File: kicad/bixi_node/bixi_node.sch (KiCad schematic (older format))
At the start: 6 parts, among them J1 RJ45, J2 Screw_Terminal_1x02, P1 CONN_01X03, U1 SP3485CN

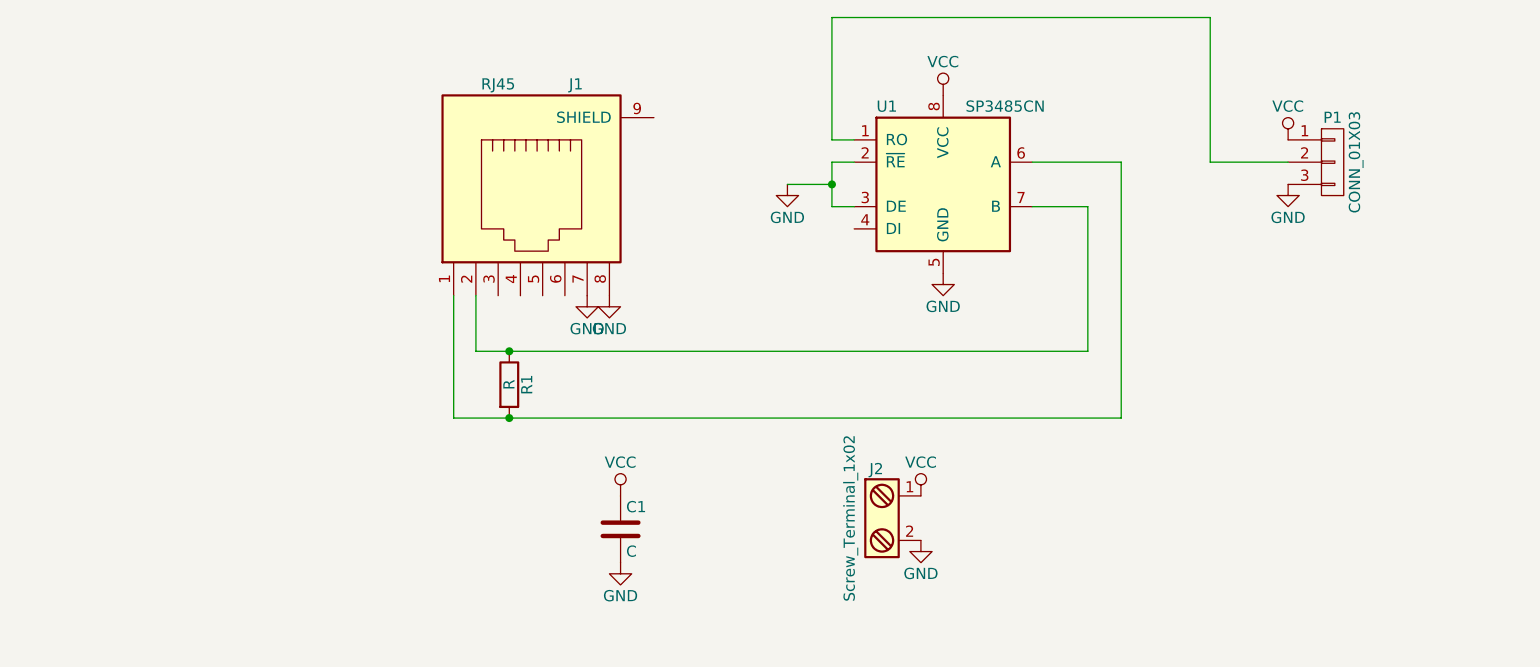
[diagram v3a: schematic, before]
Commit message: both pcb's sent to fab
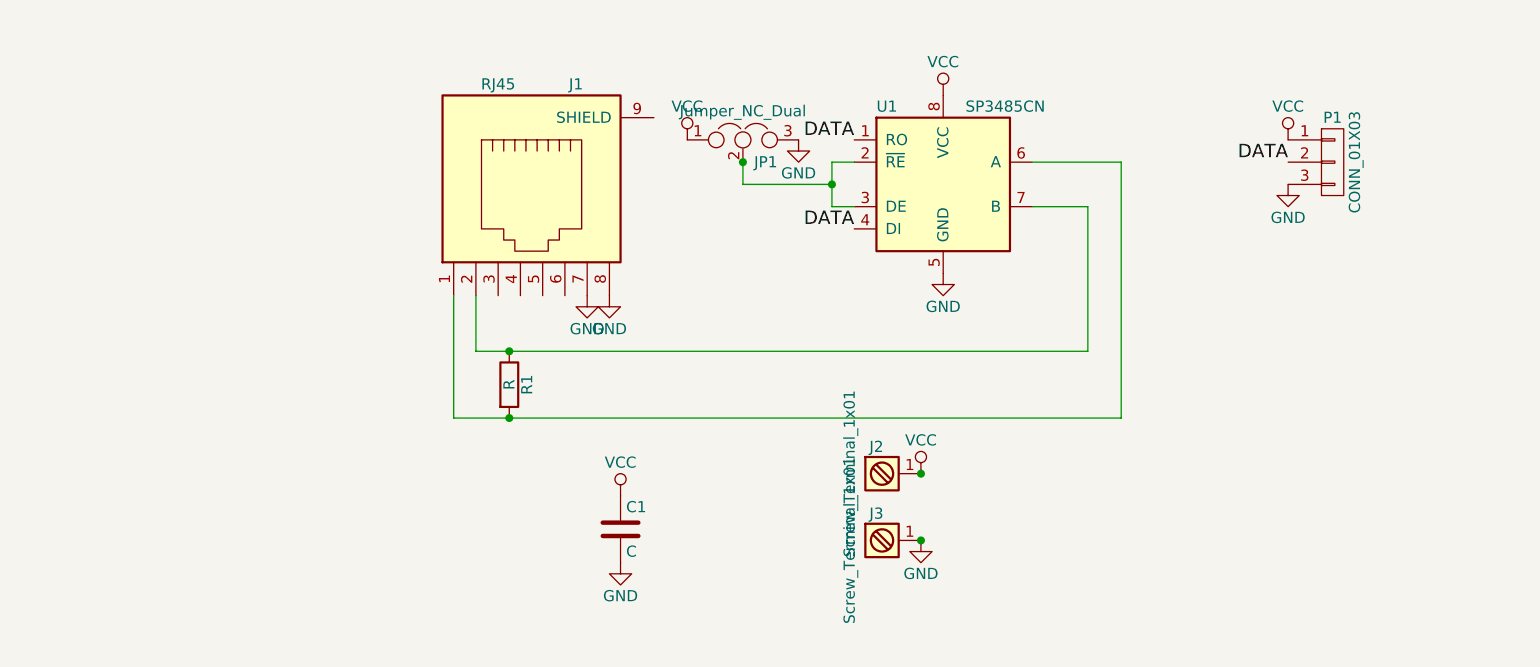
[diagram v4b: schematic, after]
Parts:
- removed J2: Screw_Terminal_1x02, custom:HB9500-2P, symbol Screw_Terminal_1x02
- added J2, J3: Screw_Terminal_1x01, custom:A116169CT_SPADE_CONNECTOR, symbol Screw_Terminal_1x01
- added JP1: Jumper_NC_Dual, custom:jumper_3_pin_fixed, symbol Jumper_NC_Dual
- P1: footprint custom:PAD_3X_OVAL -> custom:PAD_3X_OVAL_WS2812B
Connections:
- net GND: now also J3.1, JP1.3; no longer U1.2 (~RE~), U1.3 (DE)
- net VCC: now also J2.1, JP1.1
- net DATA: now reaches P1.2 (P2), U1.1 (RO)
- net DATA: now also U1.4 (DI)
- new net: JP1.2, U1.2 (~RE~), U1.3 (DE)
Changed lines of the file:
@@
+	1    0    0    -1
+$EndComp
+$Comp
+L VCC #PWR07
+U 1 1 58D6B5B6
+P 7350 3100
+F 0 "#PWR07" H 7350 2950 50  0001 C CNN
+F 1 "VCC" H 7350 3250 50  0000 C CNN
+F 2 "" H 7350 3100 50  0000 C CNN
+F 3 "" H 7350 3100 50  0000 C CNN
+	1    7350 3100
+	1    0    0    -1
+$EndComp
+$Comp
+L GND #PWR08
+U 1 1 58D6B5DA
+P 7350 3300
+F 0 "#PWR08" H 7350 3050 50  0001 C CNN
+F 1 "GND" H 7350 3150 50  0000 C CNN
+F 2 "" H 7350 3300 50  0000 C CNN
+F 3 "" H 7350 3300 50  0000 C CNN
+	1    7350 3300
+	1    0    0    -1
+$EndComp
+$Comp
+L GND #PWR09
+U 1 1 58D6B6AE
+P 5700 4900
+F 0 "#PWR09" H 5700 4650 50  0001 C CNN
+F 1 "GND" H 5700 4750 50  0000 C CNN
+F 2 "" H 5700 4900 50  0000 C CNN
+F 3 "" H 5700 4900 50  0000 C CNN
+	1    5700 4900
+	1    0    0    -1
+$EndComp
+$Comp
+L VCC #PWR010
+U 1 1 58D6B70F
+P 5700 4600
+F 0 "#PWR010" H 5700 4450 50  0001 C CNN
+F 1 "VCC" H 5700 4750 50  0000 C CNN
+F 2 "" H 5700 4600 50  0000 C CNN
+F 3 "" H 5700 4600 50  0000 C CNN
+	1    5700 4600
+	1    0    0    -1
+$EndComp
+$Comp
+L CONN_01X03 P1
+U 1 1 58D6C384
+P 7550 3200
+F 0 "P1" H 7550 3400 50  0000 C CNN
+F 1 "CONN_01X03" V 7650 3200 50  0000 C CNN
+F 2 "custom:PAD_3X_OVAL_WS2812B" H 7550 3200 50  0001 C CNN
+F 3 "" H 7550 3200 50  0000 C CNN
+	1    7550 3200
+	1    0    0    -1
+$EndComp
+$Comp
+L Screw_Terminal_1x01 J2
+U 1 1 58EA38FE
+P 5500 4600
+F 0 "J2" H 5500 4750 50  0000 C TNN
+F 1 "Screw_Terminal_1x01" V 5350 4600 50  0000 C TNN
+F 2 "custom:A116169CT_SPADE_CONNECTOR" H 5500 4475 50  0001 C CNN
+F 3 "" H 5500 4500 50  0001 C CNN
+	1    5500 4600
+	1    0    0    -1
+$EndComp
+$Comp
+L Screw_Terminal_1x01 J3
+U 1 1 58EA3975
+P 5500 4900
+F 0 "J3" H 5500 5050 50  0000 C TNN
+F 1 "Screw_Terminal_1x01" V 5350 4900 50  0000 C TNN
+F 2 "custom:A116169CT_SPADE_CONNECTOR" H 5500 4775 50  0001 C CNN
+F 3 "" H 5500 4800 50  0001 C CNN
+	1    5500 4900
+	1    0    0    -1
+$EndComp
+$Comp
+L VCC #PWR011
+U 1 1 58EA51F3
+P 4650 3100
+F 0 "#PWR011" H 4650 2950 50  0001 C CNN
+F 1 "VCC" H 4650 3250 50  0000 C CNN
+F 2 "" H 4650 3100 50  0000 C CNN
+F 3 "" H 4650 3100 50  0000 C CNN
+	1    4650 3100
+	1    0    0    -1
+$EndComp
+$Comp
+L GND #PWR012
+U 1 1 58EA5217
+P 5150 3100
+F 0 "#PWR012" H 5150 2850 50  0001 C CNN
+F 1 "GND" H 5150 2950 50  0000 C CNN
+F 2 "" H 5150 3100 50  0000 C CNN
+F 3 "" H 5150 3100 50  0000 C CNN
+	1    5150 3100
 	1    0    0    -1
 $EndComp
@@
 Connection ~ 5300 3300
 Wire Wire Line
-	5400 3100 5300 3100
+	4900 3300 5300 3300
+Connection ~ 3850 4050
+Connection ~ 3850 4350
+Connection ~ 5700 4900
+Connection ~ 5700 4600
 Wire Wire Line
-	5300 3100 5300 2550
-Wire Wire Line
-	5300 2550 7000 2550
-Wire Wire Line
-	7000 2550 7000 3200
-Wire Wire Line
-	7000 3200 7350 3200
+	4900 3300 4900 3200
+Text Label 7350 3200 2    60   ~ 0
+DATA
+Text Label 5400 3100 2    60   ~ 0
+DATA
+Text Label 5400 3500 2    60   ~ 0
+DATA
+Connection ~ 4900 3200
 $Comp
-L GND #PWR07
-U 1 1 58CE0E7E
-P 5100 3300
-F 0 "#PWR07" H 5100 3050 50  0001 C CNN
-F 1 "GND" H 5100 3150 50  0000 C CNN
-F 2 "" H 5100 3300 50  0000 C CNN
-F 3 "" H 5100 3300 50  0000 C CNN
-	1    5100 3300
+L Jumper_NC_Dual JP1
+U 1 1 58EA59A3
+P 4900 3100
+F 0 "JP1" H 4950 3000 50  0000 L CNN
+F 1 "Jumper_NC_Dual" H 4900 3200 50  0000 C BNN
+F 2 "custom:jumper_3_pin_fixed" H 4900 3100 50  0001 C CNN
+F 3 "" H 4900 3100 50  0000 C CNN
+	1    4900 3100
 	1    0    0    -1
 $EndComp
-Wire Wire Line
-	5300 3300 5100 3300
-$Comp
-L VCC #PWR08
-U 1 1 58D6B5B6
-P 7350 3100
-F 0 "#PWR08" H 7350 2950 50  0001 C CNN
-F 1 "VCC" H 7350 3250 50  0000 C CNN
-F 2 "" H 7350 3100 50  0000 C CNN
-F 3 "" H 7350 3100 50  0000 C CNN
-	1    7350 3100
-	1    0    0    -1
-$EndComp
-$Comp
-L GND #PWR09
-U 1 1 58D6B5DA
-P 7350 3300
-F 0 "#PWR09" H 7350 3050 50  0001 C CNN
-F 1 "GND" H 7350 3150 50  0000 C CNN
-F 2 "" H 7350 3300 50  0000 C CNN
-F 3 "" H 7350 3300 50  0000 C CNN
-	1    7350 3300
-	1    0    0    -1
-$EndComp
-$Comp
-L GND #PWR010
-U 1 1 58D6B6AE
-P 5700 4900
-F 0 "#PWR010" H 5700 4650 50  0001 C CNN
-F 1 "GND" H 5700 4750 50  0000 C CNN
-F 2 "" H 5700 4900 50  0000 C CNN
-F 3 "" H 5700 4900 50  0000 C CNN
-	1    5700 4900
-	1    0    0    -1
-$EndComp
-$Comp
-L VCC #PWR011
-U 1 1 58D6B70F
-P 5700 4700
-F 0 "#PWR011" H 5700 4550 50  0001 C CNN
-F 1 "VCC" H 5700 4850 50  0000 C CNN
-F 2 "" H 5700 4700 50  0000 C CNN
-F 3 "" H 5700 4700 50  0000 C CNN
-	1    5700 4700
-	1    0    0    -1
-$EndComp
-$Comp
-L CONN_01X03 P1
-U 1 1 58D6C384
-P 7550 3200
-F 0 "P1" H 7550 3400 50  0000 C CNN
-F 1 "CONN_01X03" V 7650 3200 50  0000 C CNN
-F 2 "custom:PAD_3X_OVAL" H 7550 3200 50  0001 C CNN
-F 3 "" H 7550 3200 50  0000 C CNN
-	1    7550 3200
-	1    0    0    -1
-$EndComp
-Connection ~ 3850 4050
-Connection ~ 3850 4350
-$Comp
-L Screw_Terminal_1x02 J2
-U 1 1 58E151AB
-P 5500 4800
-F 0 "J2" H 5500 5050 50  0000 C TNN
-F 1 "Screw_Terminal_1x02" V 5350 4800 50  0000 C TNN
-F 2 "custom:HB9500-2P" H 5500 4575 50  0001 C CNN
-F 3 "" H 5475 4800 50  0001 C CNN
-	1    5500 4800
-	1    0    0    -1
-$EndComp

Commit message: v2 pcb
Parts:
- C1: footprint Resistors_THT:Resistor_Horizontal_RM7mm -> Capacitors_THT:C_Disc_D3.0mm_W2.0mm_P2.50mm
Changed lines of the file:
@@
 F 0 "C1" H 4375 4950 50  0000 L CNN
 F 1 "C" H 4375 4750 50  0000 L CNN
-F 2 "Resistors_THT:Resistor_Horizontal_RM7mm" H 4388 4700 50  0001 C CNN
+F 2 "Capacitors_THT:C_Disc_D3.0mm_W2.0mm_P2.50mm" H 4388 4700 50  0001 C CNN
 F 3 "" H 4350 4850 50  0000 C CNN
 	1    4350 4850

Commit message: bixi node updates
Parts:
- C1: footprint Capacitors_THT:C_Disc_D3.0mm_W2.0mm_P2.50mm -> Capacitors_THT:C_Axial_L3.8mm_D2.6mm_P7.50mm_Horizontal
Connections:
- net DATA: now also J1.3
- net VCC: now also J1.5, J1.6
- net DATA_DIFF_A: now reaches J1.1, R1.2, U1.6 (A)
- net DATA_DIFF_B: now reaches J1.2, R1.1, U1.7 (B)
- net MODE: now reaches JP1.2, U1.2 (~RE~), U1.3 (DE)
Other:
- moved on the sheet: J2, J3, JP1, P1

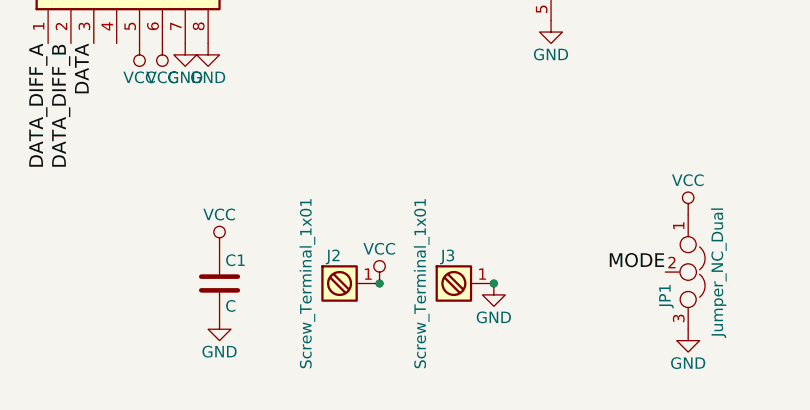
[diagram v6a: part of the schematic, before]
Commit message: v3 boards almost complete. added xcvr breakout, passthrough boards
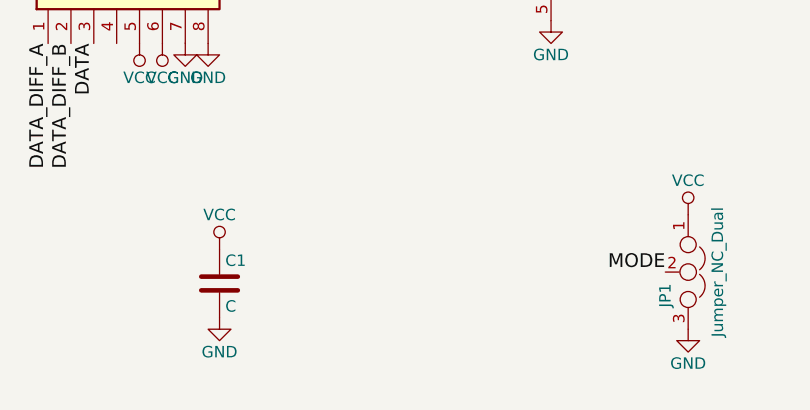
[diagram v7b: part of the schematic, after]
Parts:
- removed J2, J3: Screw_Terminal_1x01, custom:A116169CT_SPADE_CONNECTOR, symbol Screw_Terminal_1x01
- P1: footprint custom:PAD_3X_OVAL_WS2812B -> Connectors_JST:JST_EH_S03B-EH_03x2.50mm_Angled
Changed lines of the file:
@@
 $EndComp
 $Comp
-L GND #PWR10
+L GND #PWR01
 U 1 1 58CE067C
 P 5800 3700
-F 0 "#PWR10" H 5800 3450 50  0001 C CNN
+F 0 "#PWR01" H 5800 3450 50  0001 C CNN
 F 1 "GND" H 5800 3550 50  0000 C CNN
 F 2 "" H 5800 3700 50  0000 C CNN
@@
 $EndComp
 $Comp
-L GND #PWR3
+L GND #PWR02
 U 1 1 58CE0696
 P 4200 3800
-F 0 "#PWR3" H 4200 3550 50  0001 C CNN
+F 0 "#PWR02" H 4200 3550 50  0001 C CNN
 F 1 "GND" H 4200 3650 50  0000 C CNN
 F 2 "" H 4200 3800 50  0000 C CNN
@@
 $EndComp
 $Comp
-L GND #PWR4
+L GND #PWR03
 U 1 1 58CE06B0
 P 4300 3800
-F 0 "#PWR4" H 4300 3550 50  0001 C CNN
+F 0 "#PWR03" H 4300 3550 50  0001 C CNN
 F 1 "GND" H 4300 3650 50  0000 C CNN
 F 2 "" H 4300 3800 50  0000 C CNN
@@
 $EndComp
 $Comp
-L VCC #PWR9
+L VCC #PWR04
 U 1 1 58CE06CA
 P 5800 2900
-F 0 "#PWR9" H 5800 2750 50  0001 C CNN
+F 0 "#PWR04" H 5800 2750 50  0001 C CNN
 F 1 "VCC" H 5800 3050 50  0000 C CNN
 F 2 "" H 5800 2900 50  0000 C CNN
@@
 $EndComp
 $Comp
-L VCC #PWR5
+L VCC #PWR05
 U 1 1 58CE07F1
 P 4350 4700
-F 0 "#PWR5" H 4350 4550 50  0001 C CNN
+F 0 "#PWR05" H 4350 4550 50  0001 C CNN
 F 1 "VCC" H 4350 4850 50  0000 C CNN
 F 2 "" H 4350 4700 50  0000 C CNN
@@
 $EndComp
 $Comp
-L GND #PWR6
+L GND #PWR06
 U 1 1 58CE0C7F
 P 4350 5000
-F 0 "#PWR6" H 4350 4750 50  0001 C CNN
+F 0 "#PWR06" H 4350 4750 50  0001 C CNN
 F 1 "GND" H 4350 4850 50  0000 C CNN
 F 2 "" H 4350 5000 50  0000 C CNN
@@
 $EndComp
 $Comp
-L VCC #PWR13
+L VCC #PWR07
 U 1 1 58D6B5B6
 P 8050 3200
-F 0 "#PWR13" H 8050 3050 50  0001 C CNN
+F 0 "#PWR07" H 8050 3050 50  0001 C CNN
 F 1 "VCC" H 8050 3350 50  0000 C CNN
 F 2 "" H 8050 3200 50  0000 C CNN
@@
 $EndComp
 $Comp
-L GND #PWR14
+L GND #PWR08
 U 1 1 58D6B5DA
 P 8050 3400
-F 0 "#PWR14" H 8050 3150 50  0001 C CNN
+F 0 "#PWR08" H 8050 3150 50  0001 C CNN
 F 1 "GND" H 8050 3250 50  0000 C CNN
 F 2 "" H 8050 3400 50  0000 C CNN
 F 3 "" H 8050 3400 50  0000 C CNN
 	1    8050 3400
-	1    0    0    -1
-$EndComp
-$Comp
-L GND #PWR8
-U 1 1 58D6B6AE
-P 5550 4850
-F 0 "#PWR8" H 5550 4600 50  0001 C CNN
-F 1 "GND" H 5550 4700 50  0000 C CNN
-F 2 "" H 5550 4850 50  0000 C CNN
-F 3 "" H 5550 4850 50  0000 C CNN
-	1    5550 4850
-	1    0    0    -1
-$EndComp
-$Comp
-L VCC #PWR7
-U 1 1 58D6B70F
-P 5050 4850
-F 0 "#PWR7" H 5050 4700 50  0001 C CNN
-F 1 "VCC" H 5050 5000 50  0000 C CNN
-F 2 "" H 5050 4850 50  0000 C CNN
-F 3 "" H 5050 4850 50  0000 C CNN
-	1    5050 4850
 	1    0    0    -1
 $EndComp
@@
 F 0 "P1" H 8250 3500 50  0000 C CNN
 F 1 "CONN_01X03" V 8350 3300 50  0000 C CNN
-F 2 "custom:PAD_3X_OVAL_WS2812B" H 8250 3300 50  0001 C CNN
+F 2 "Connectors_JST:JST_EH_S03B-EH_03x2.50mm_Angled" H 8250 3300 50  0001 C CNN
 F 3 "" H 8250 3300 50  0000 C CNN
 	1    8250 3300
@@
 $EndComp
 $Comp
-L Screw_Terminal_1x01 J2
-U 1 1 58EA38FE
-P 4850 4850
-F 0 "J2" H 4850 5000 50  0000 C TNN
-F 1 "Screw_Terminal_1x01" V 4700 4850 50  0000 C TNN
-F 2 "custom:A116169CT_SPADE_CONNECTOR" H 4850 4725 50  0001 C CNN
-F 3 "" H 4850 4750 50  0001 C CNN
-	1    4850 4850
-	1    0    0    -1
-$EndComp
-$Comp
-L Screw_Terminal_1x01 J3
-U 1 1 58EA3975
-P 5350 4850
-F 0 "J3" H 5350 5000 50  0000 C TNN
-F 1 "Screw_Terminal_1x01" V 5200 4850 50  0000 C TNN
-F 2 "custom:A116169CT_SPADE_CONNECTOR" H 5350 4725 50  0001 C CNN
-F 3 "" H 5350 4750 50  0001 C CNN
-	1    5350 4850
-	1    0    0    -1
-$EndComp
-$Comp
-L VCC #PWR11
+L VCC #PWR011
 U 1 1 58EA51F3
 P 6400 4550
-F 0 "#PWR11" H 6400 4400 50  0001 C CNN
+F 0 "#PWR011" H 6400 4400 50  0001 C CNN
 F 1 "VCC" H 6400 4700 50  0000 C CNN
 F 2 "" H 6400 4550 50  0000 C CNN
@@
 $EndComp
 $Comp
-L GND #PWR12
+L GND #PWR012
 U 1 1 58EA5217
 P 6400 5050
-F 0 "#PWR12" H 6400 4800 50  0001 C CNN
+F 0 "#PWR012" H 6400 4800 50  0001 C CNN
 F 1 "GND" H 6400 4900 50  0000 C CNN
 F 2 "" H 6400 5050 50  0000 C CNN
@@
 	1    0    0    -1
 $EndComp
-Connection ~ 5550 4850
-Connection ~ 5050 4850
 Text Label 5400 3100 2    60   ~ 0
 DATA
@@
 MODE
 $Comp
-L VCC #PWR2
+L VCC #PWR013
 U 1 1 5902A84B
 P 4100 3800
-F 0 "#PWR2" H 4100 3650 50  0001 C CNN
+F 0 "#PWR013" H 4100 3650 50  0001 C CNN
 F 1 "VCC" H 4100 3950 50  0000 C CNN
 F 2 "" H 4100 3800 50  0000 C CNN
@@
 $EndComp
 $Comp
-L VCC #PWR1
+L VCC #PWR014
 U 1 1 5902A94D
 P 4000 3800
-F 0 "#PWR1" H 4000 3650 50  0001 C CNN
+F 0 "#PWR014" H 4000 3650 50  0001 C CNN
 F 1 "VCC" H 4000 3950 50  0000 C CNN
 F 2 "" H 4000 3800 50  0000 C CNN

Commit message: v3 pcb's plotted, ready for fab
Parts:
- P1: footprint Connectors_JST:JST_EH_S03B-EH_03x2.50mm_Angled -> custom:PAD_3X_OVAL_WS2812B
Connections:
- net DATA: no longer J1.3
- net VCC: no longer J1.5, J1.6
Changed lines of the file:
@@
 F 0 "P1" H 8250 3500 50  0000 C CNN
 F 1 "CONN_01X03" V 8350 3300 50  0000 C CNN
-F 2 "Connectors_JST:JST_EH_S03B-EH_03x2.50mm_Angled" H 8250 3300 50  0001 C CNN
+F 2 "custom:PAD_3X_OVAL_WS2812B" H 8250 3300 50  0001 C CNN
 F 3 "" H 8250 3300 50  0000 C CNN
 	1    8250 3300
@@
 $EndComp
 $Comp
-L VCC #PWR011
+L VCC #PWR09
 U 1 1 58EA51F3
 P 6400 4550
-F 0 "#PWR011" H 6400 4400 50  0001 C CNN
+F 0 "#PWR09" H 6400 4400 50  0001 C CNN
 F 1 "VCC" H 6400 4700 50  0000 C CNN
 F 2 "" H 6400 4550 50  0000 C CNN
@@
 $EndComp
 $Comp
-L GND #PWR012
+L GND #PWR010
 U 1 1 58EA5217
 P 6400 5050
-F 0 "#PWR012" H 6400 4800 50  0001 C CNN
+F 0 "#PWR010" H 6400 4800 50  0001 C CNN
 F 1 "GND" H 6400 4900 50  0000 C CNN
 F 2 "" H 6400 5050 50  0000 C CNN
@@
 Text Label 3700 3800 3    60   ~ 0
 DATA_DIFF_B
-Text Label 3800 3800 3    60   ~ 0
-DATA
 Text Label 2300 3350 2    60   ~ 0
 DATA_DIFF_A
@@
 Text Label 6300 4800 2    60   ~ 0
 MODE
-$Comp
-L VCC #PWR013
-U 1 1 5902A84B
-P 4100 3800
-F 0 "#PWR013" H 4100 3650 50  0001 C CNN
-F 1 "VCC" H 4100 3950 50  0000 C CNN
-F 2 "" H 4100 3800 50  0000 C CNN
-F 3 "" H 4100 3800 50  0000 C CNN
-	1    4100 3800
-	-1   0    0    1
-$EndComp
-$Comp
-L VCC #PWR014
-U 1 1 5902A94D
-P 4000 3800
-F 0 "#PWR014" H 4000 3650 50  0001 C CNN
-F 1 "VCC" H 4000 3950 50  0000 C CNN
-F 2 "" H 4000 3800 50  0000 C CNN
-F 3 "" H 4000 3800 50  0000 C CNN
-	1    4000 3800
-	-1   0    0    1
-$EndComp
 $EndSCHEMATC
